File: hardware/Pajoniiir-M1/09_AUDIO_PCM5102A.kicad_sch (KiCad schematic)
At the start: 23 parts, among them J4 RCA LEFT TBD-MECH, J5 RCA RIGHT TBD-MECH, J6 3.5MM LINE OUT DNP, U5 PCM5102APWR

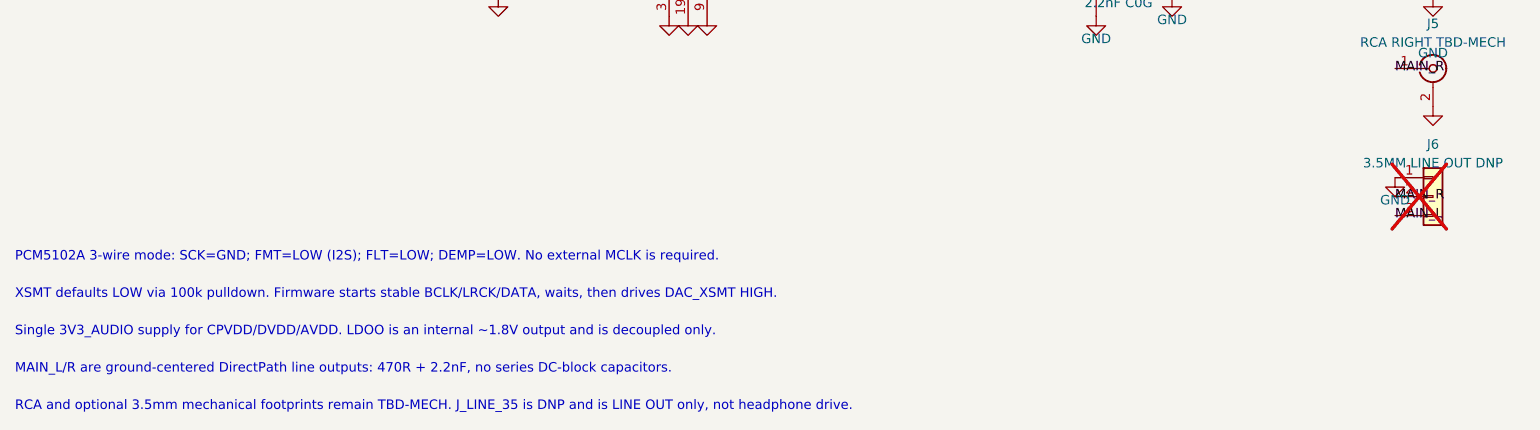
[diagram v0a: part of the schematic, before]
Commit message: mechanical: remove optional J6 from Rev A
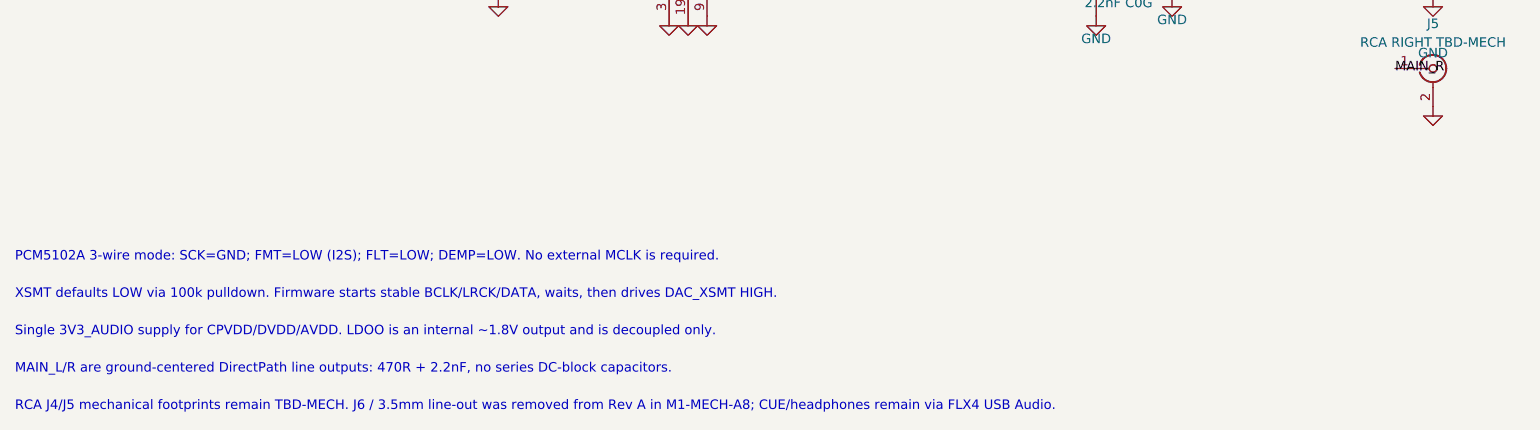
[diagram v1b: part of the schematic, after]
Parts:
- removed J6: 3.5MM LINE OUT DNP, symbol Connector_Generic:Conn_01x03
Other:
- note added: "RCA J4/J5 mechanical footprints remain TBD-MECH. J6 / 3.5mm line-out was removed from Rev A in M1-MECH-A8; CUE/headphones remain via FLX4 USB Audio."
- note removed: "RCA and optional 3.5mm mechanical footprints remain TBD-MECH. J_LINE_35 is DNP and is LINE OUT only, not headphone drive."
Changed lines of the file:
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@@
     (instances (project "Pajoniiir-M1" (path "/2c8dd352-b7b8-4d9e-8f93-5dd43be2a100/31000009-6b2a-4a3a-8c91-000000000009" (reference "#PWR0915") (unit 1))))
-  )
-  (symbol
-    (lib_id "Connector_Generic:Conn_01x03") (at 224.79 121.92 0) (unit 1)
-    (exclude_from_sim no) (in_bom yes) (on_board yes) (dnp yes)
-    (property "Reference" "J6" (at 224.79 114.92 0) (effects (font (size 1.27 1.27))))
-    (property "Value" "3.5MM LINE OUT DNP" (at 224.79 117.42 0) (effects (font (size 1.27 1.27))))
-    (property "Footprint" "" (at 224.79 121.92 0) (effects (font (size 1.27 1.27)) (hide yes)))
-    (property "Datasheet" "~" (at 224.79 121.92 0) (effects (font (size 1.27 1.27)) (hide yes)))
-    (pin "1") (pin "2") (pin "3")
-    (instances (project "Pajoniiir-M1" (path "/2c8dd352-b7b8-4d9e-8f93-5dd43be2a100/31000009-6b2a-4a3a-8c91-000000000009" (reference "J6") (unit 1))))
-  )
-  (label "MAIN_L" (at 219.71 124.46 0) (effects (font (size 1.27 1.27))))
-  (label "MAIN_R" (at 219.71 121.92 0) (effects (font (size 1.27 1.27))))
-  (symbol
-    (lib_id "power:GND") (at 219.71 119.38 0) (unit 1)
-    (exclude_from_sim no) (in_bom yes) (on_board yes) (dnp no)
-    (property "Reference" "#PWR0916" (at 219.71 125.38 0) (effects (font (size 1.27 1.27)) (hide yes)))
-    (property "Value" "GND" (at 219.71 122.38 0) (effects (font (size 1.27 1.27))))
-    (property "Footprint" "" (at 219.71 119.38 0) (effects (font (size 1.27 1.27)) (hide yes)))
-    (property "Datasheet" "" (at 219.71 119.38 0) (effects (font (size 1.27 1.27)) (hide yes)))
-    (pin "1")
-    (instances (project "Pajoniiir-M1" (path "/2c8dd352-b7b8-4d9e-8f93-5dd43be2a100/31000009-6b2a-4a3a-8c91-000000000009" (reference "#PWR0916") (unit 1))))
   )
   (text "PCM5102A 3-wire mode: SCK=GND; FMT=LOW (I2S); FLT=LOW; DEMP=LOW. No external MCLK is required." (exclude_from_sim no) (at 35 130 0) (effects (font (size 1.27 1.27)) (justify left)))
@@
   (text "Single 3V3_AUDIO supply for CPVDD/DVDD/AVDD. LDOO is an internal ~1.8V output and is decoupled only." (exclude_from_sim no) (at 35 140 0) (effects (font (size 1.27 1.27)) (justify left)))
   (text "MAIN_L/R are ground-centered DirectPath line outputs: 470R + 2.2nF, no series DC-block capacitors." (exclude_from_sim no) (at 35 145 0) (effects (font (size 1.27 1.27)) (justify left)))
-  (text "RCA and optional 3.5mm mechanical footprints remain TBD-MECH. J_LINE_35 is DNP and is LINE OUT only, not headphone drive." (exclude_from_sim no) (at 35 150 0) (effects (font (size 1.27 1.27)) (justify left)))
+  (text "RCA J4/J5 mechanical footprints remain TBD-MECH. J6 / 3.5mm line-out was removed from Rev A in M1-MECH-A8; CUE/headphones remain via FLX4 USB Audio." (exclude_from_sim no) (at 35 150 0) (effects (font (size 1.27 1.27)) (justify left)))
   (symbol
     (lib_id "power:PWR_FLAG")

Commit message: mechanical: lock USB and RCA footprints
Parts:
- J4: value RCA LEFT TBD-MECH -> KLPX-0848A-2-W-G; footprint (none) -> Pajoniiir-M1:Kycon_KLPX-0848A-2-x-G
- J5: value RCA RIGHT TBD-MECH -> KLPX-0848A-2-R-G; footprint (none) -> Pajoniiir-M1:Kycon_KLPX-0848A-2-x-G
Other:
- note added: "RCA J4/J5 Kycon KLPX-0848A gold-family footprints are locked; final panel XY/cutouts remain open. J6 / 3.5mm line-out was removed from Rev A in M1-MECH-A8; CUE/headphones remain via FLX4 USB Audio."
- note removed: "RCA J4/J5 mechanical footprints remain TBD-MECH. J6 / 3.5mm line-out was removed from Rev A in M1-MECH-A8; CUE/headphones remain via FLX4 USB Audio."
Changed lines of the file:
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@@
     (exclude_from_sim no) (in_bom yes) (on_board yes) (dnp no)
     (property "Reference" "J4" (at 224.79 84.01 0) (effects (font (size 1.27 1.27))))
-    (property "Value" "RCA LEFT TBD-MECH" (at 224.79 86.51 0) (effects (font (size 1.27 1.27))))
-    (property "Footprint" "" (at 224.79 90.17 0) (effects (font (size 1.27 1.27)) (hide yes)))
-    (property "Datasheet" "~" (at 224.79 90.17 0) (effects (font (size 1.27 1.27)) (hide yes)))
+    (property "Value" "KLPX-0848A-2-W-G" (at 224.79 86.51 0) (effects (font (size 1.27 1.27))))
+    (property "Footprint" "Pajoniiir-M1:Kycon_KLPX-0848A-2-x-G" (at 224.79 90.17 0) (effects (font (size 1.27 1.27)) (hide yes)))
+    (property "Datasheet" "https://www.kycon.com/Pub_Eng_Draw/KLPX-0848A-2-x-G.pdf" (at 224.79 90.17 0) (effects (font (size 1.27 1.27)) (hide yes)))
     (pin "1") (pin "2")
     (instances (project "Pajoniiir-M1" (path "/2c8dd352-b7b8-4d9e-8f93-5dd43be2a100/31000009-6b2a-4a3a-8c91-000000000009" (reference "J4") (unit 1))))
@@
     (exclude_from_sim no) (in_bom yes) (on_board yes) (dnp no)
     (property "Reference" "J5" (at 224.79 98.775 0) (effects (font (size 1.27 1.27))))
-    (property "Value" "RCA RIGHT TBD-MECH" (at 224.79 101.275 0) (effects (font (size 1.27 1.27))))
-    (property "Footprint" "" (at 224.79 104.775 0) (effects (font (size 1.27 1.27)) (hide yes)))
-    (property "Datasheet" "~" (at 224.79 104.775 0) (effects (font (size 1.27 1.27)) (hide yes)))
+    (property "Value" "KLPX-0848A-2-R-G" (at 224.79 101.275 0) (effects (font (size 1.27 1.27))))
+    (property "Footprint" "Pajoniiir-M1:Kycon_KLPX-0848A-2-x-G" (at 224.79 104.775 0) (effects (font (size 1.27 1.27)) (hide yes)))
+    (property "Datasheet" "https://www.kycon.com/Pub_Eng_Draw/KLPX-0848A-2-x-G.pdf" (at 224.79 104.775 0) (effects (font (size 1.27 1.27)) (hide yes)))
     (pin "1") (pin "2")
     (instances (project "Pajoniiir-M1" (path "/2c8dd352-b7b8-4d9e-8f93-5dd43be2a100/31000009-6b2a-4a3a-8c91-000000000009" (reference "J5") (unit 1))))
@@
   (text "Single 3V3_AUDIO supply for CPVDD/DVDD/AVDD. LDOO is an internal ~1.8V output and is decoupled only." (exclude_from_sim no) (at 35 140 0) (effects (font (size 1.27 1.27)) (justify left)))
   (text "MAIN_L/R are ground-centered DirectPath line outputs: 470R + 2.2nF, no series DC-block capacitors." (exclude_from_sim no) (at 35 145 0) (effects (font (size 1.27 1.27)) (justify left)))
-  (text "RCA J4/J5 mechanical footprints remain TBD-MECH. J6 / 3.5mm line-out was removed from Rev A in M1-MECH-A8; CUE/headphones remain via FLX4 USB Audio." (exclude_from_sim no) (at 35 150 0) (effects (font (size 1.27 1.27)) (justify left)))
+  (text "RCA J4/J5 Kycon KLPX-0848A gold-family footprints are locked; final panel XY/cutouts remain open. J6 / 3.5mm line-out was removed from Rev A in M1-MECH-A8; CUE/headphones remain via FLX4 USB Audio." (exclude_from_sim no) (at 35 150 0) (effects (font (size 1.27 1.27)) (justify left)))
   (symbol
     (lib_id "power:PWR_FLAG")
